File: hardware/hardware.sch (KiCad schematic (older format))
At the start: 5 parts

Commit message: 3.3V Voltage Regulator.
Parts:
- removed U?: L78L05_SOT89, Package_TO_SOT_SMD:SOT-89-3, symbol Regulator_Linear:L78L05_SOT89
- added C2: 0.1μF, symbol Device:C
- added C3: 1μF, symbol Device:C
- added C?: 10μF, symbol Device:CP
- added D?: M7, symbol Device:D
- added R1: 1.5k, symbol Device:R
- added R2: 1k, symbol Device:R
- added U3: LM317A, Package_TO_SOT_SMD:TO-252-2, symbol Regulator_Linear:LM317_3PinPackage
- gave numbers to parts that had none: 4
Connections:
- net labels added: Vdd
- wire segments 20 -> 49
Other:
- note added: "3.3V Voltage Regulator \w Improved Ripple Rejection"
- moved on the sheet: C1, J1, U1, U2

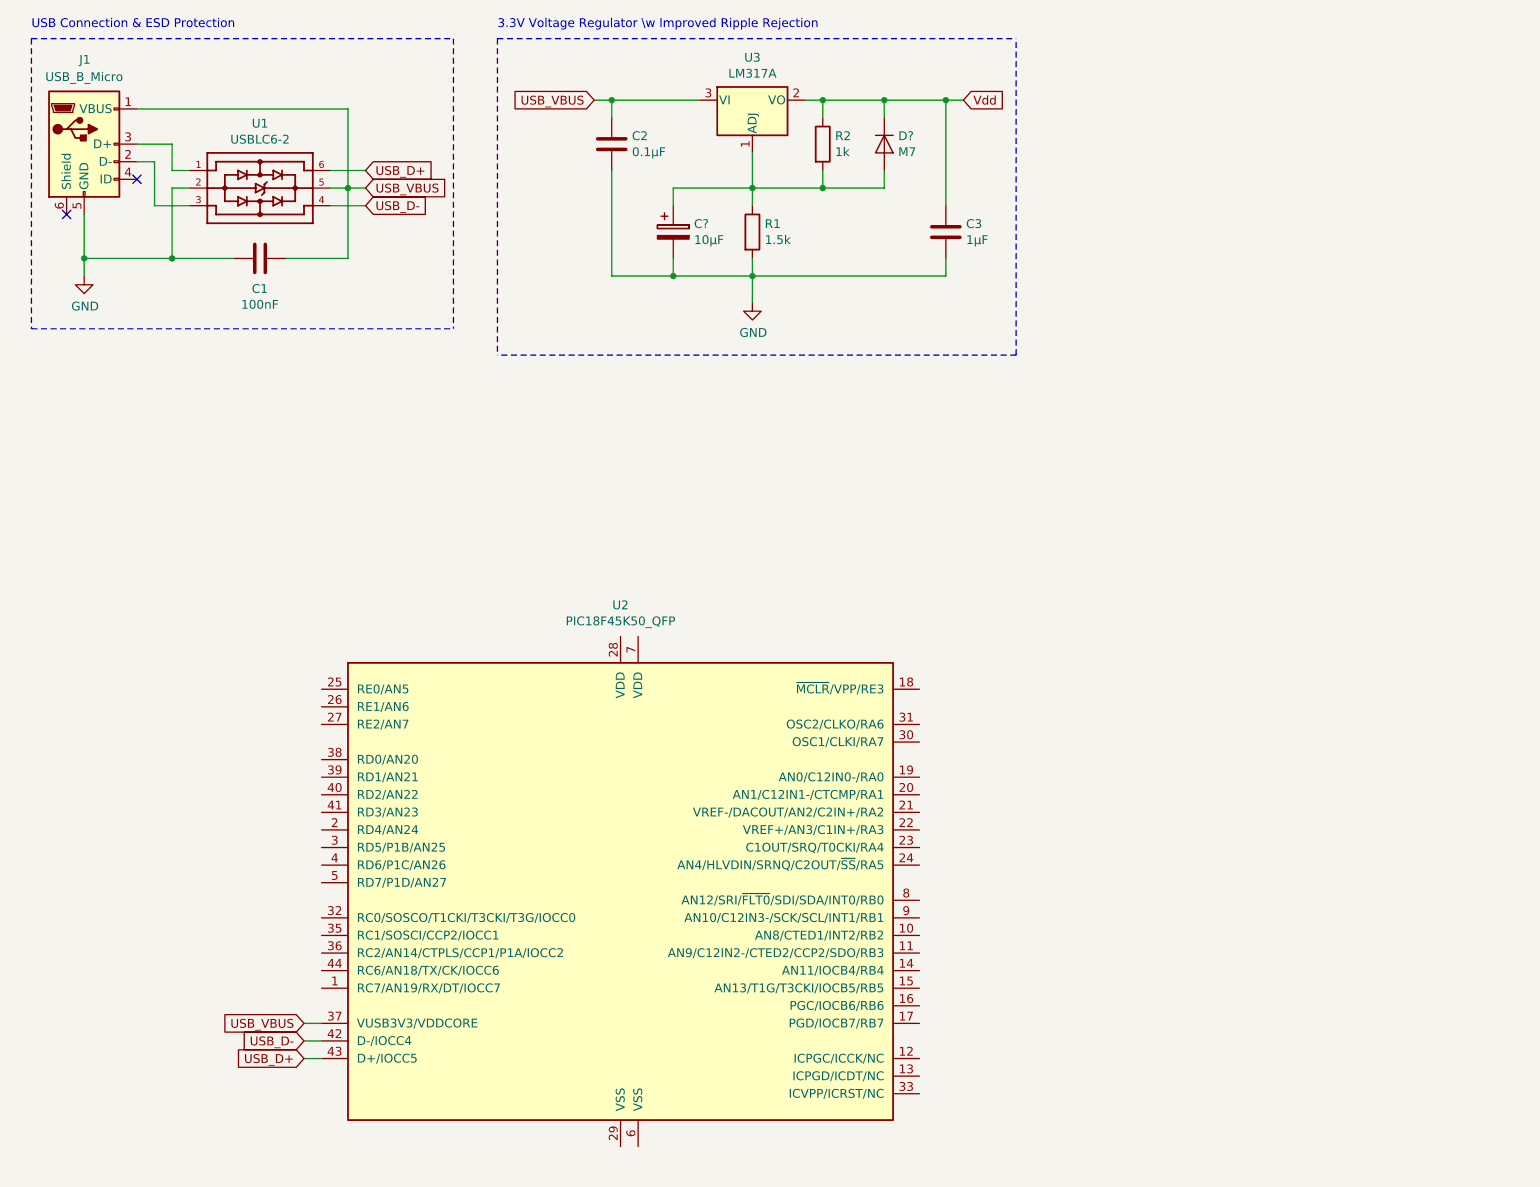
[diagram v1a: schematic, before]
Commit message: Battery protection circuit.
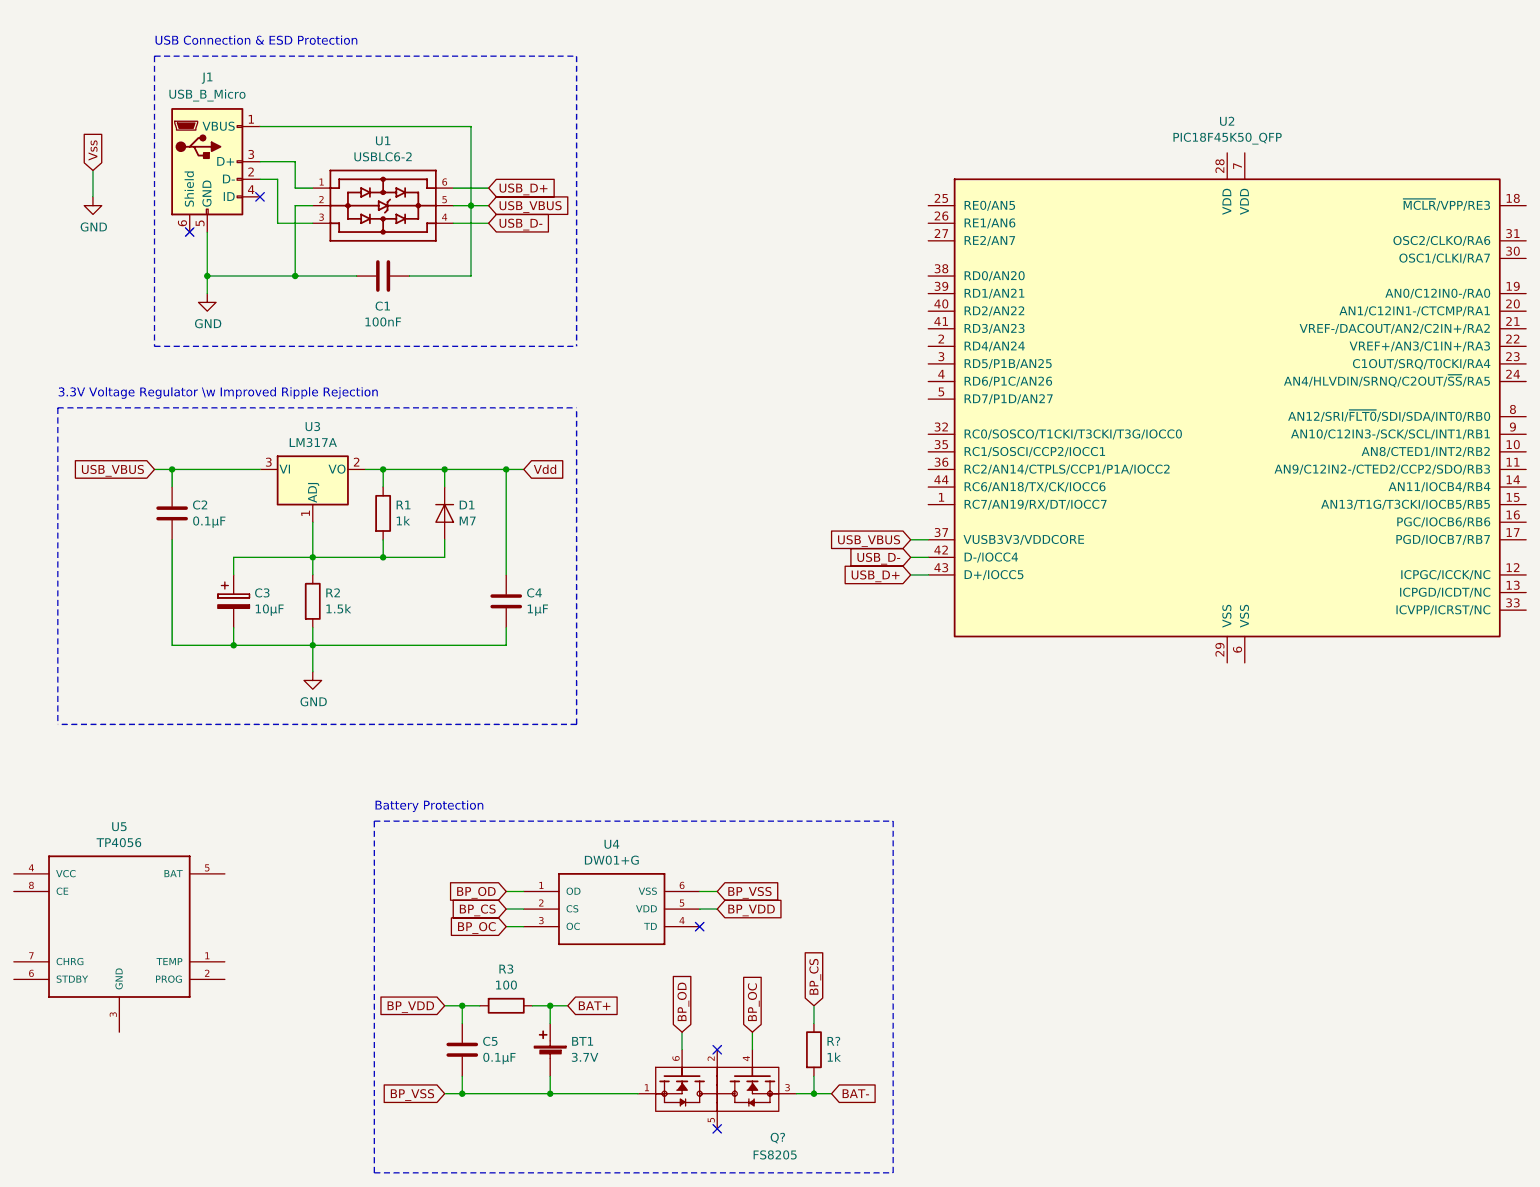
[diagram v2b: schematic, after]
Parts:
- added BT1: 3.7V, symbol Device:Battery_Cell
- added C5: 0.1μF, symbol Device:C
- added Q?: FS8205, Package_TO_SOT_SMD:TSOT-23-6_HandSoldering, symbol Missing:FS8205
- added R3: 100, symbol Device:R
- added R?: 1k, symbol Device:R
- added U4: DW01+G, Package_TO_SOT_SMD:TSOT-23-6_HandSoldering, symbol Missing:DW01
- added U5: TP4056, Package_SO:SSOP-8_2.95x2.8mm_P0.65mm, symbol Missing:TP4056
- gave numbers to parts that had none: 2
- renumbered C3 to C4, R2 to R1, R1 to R2
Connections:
- new net BAT+: BT1.1 (+), R3.1
- new net BAT-: Q?.3, R?.2
- new net BP_CS: R?.1, U4.2 (CS)
- new net BP_OC: Q?.4, U4.3 (OC)
- new net BP_OD: Q?.6, U4.1 (OD)
- new net BP_VDD: C5.1, R3.2, U4.5 (VDD)
- new net BP_VSS: BT1.2 (-), C5.2, Q?.1, U4.6 (VSS)
- no-connect marks 2 -> 5
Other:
- note added: "Battery Protection"
- moved on the sheet: C1, C2, C3, C4, D1, J1, R1, R2, U1, U2, U3

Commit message: Battery management circuit.
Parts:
- added C6, C7: 10μF, symbol Device:C
- added D2: GHC-YR, symbol Device:LED
- added D3: BHC-ZL, symbol Device:LED
- added D4: ZMM5V1, Diode_SMD:D_MiniMELF_Handsoldering, symbol Device:D_Zener
- added R4, R6: 68, symbol Device:R
- added R5: 180, symbol Device:R
- added R7: 2k, symbol Device:R
- gave numbers to parts that had none: 2
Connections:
- net BP_VSS is gone; now on net GND: BT1.2 (-), C5.2, Q1.1, U4.6 (VSS)
- net BAT+: now also R3.2, U5.5 (BAT), C7.1; no longer R3.1
- net BP_VDD: now also C2.1, R3.1, U3.3 (VI); no longer R3.2
- net GND: now also U5.1 (TEMP), U5.3 (GND), C6.2, C7.2, D4.2 (A), R7.2
- net USB_VBUS: now also R5.2; no longer C2.1, U3.3 (VI)
- net at U5.2 (PROG): now also R7.1
- net at U5.4 (VCC): now also U5.8 (CE), C6.1, D2.2 (A), D3.2 (A), D4.1 (K), R5.1
- net at U5.6 (STDBY): now also R4.1
- net at U5.7 (CHRG): now also R6.1
- net BAT-: no longer names the net of Q1.3, R8.2
- new net: D2.1 (K), R4.2
- new net: D3.1 (K), R6.2
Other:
- note added: "580mA Battery Management"
- moved on the sheet: BT1, C1, C2, C3, C4, C5, D1, J1, Q1, R1, R2, R3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

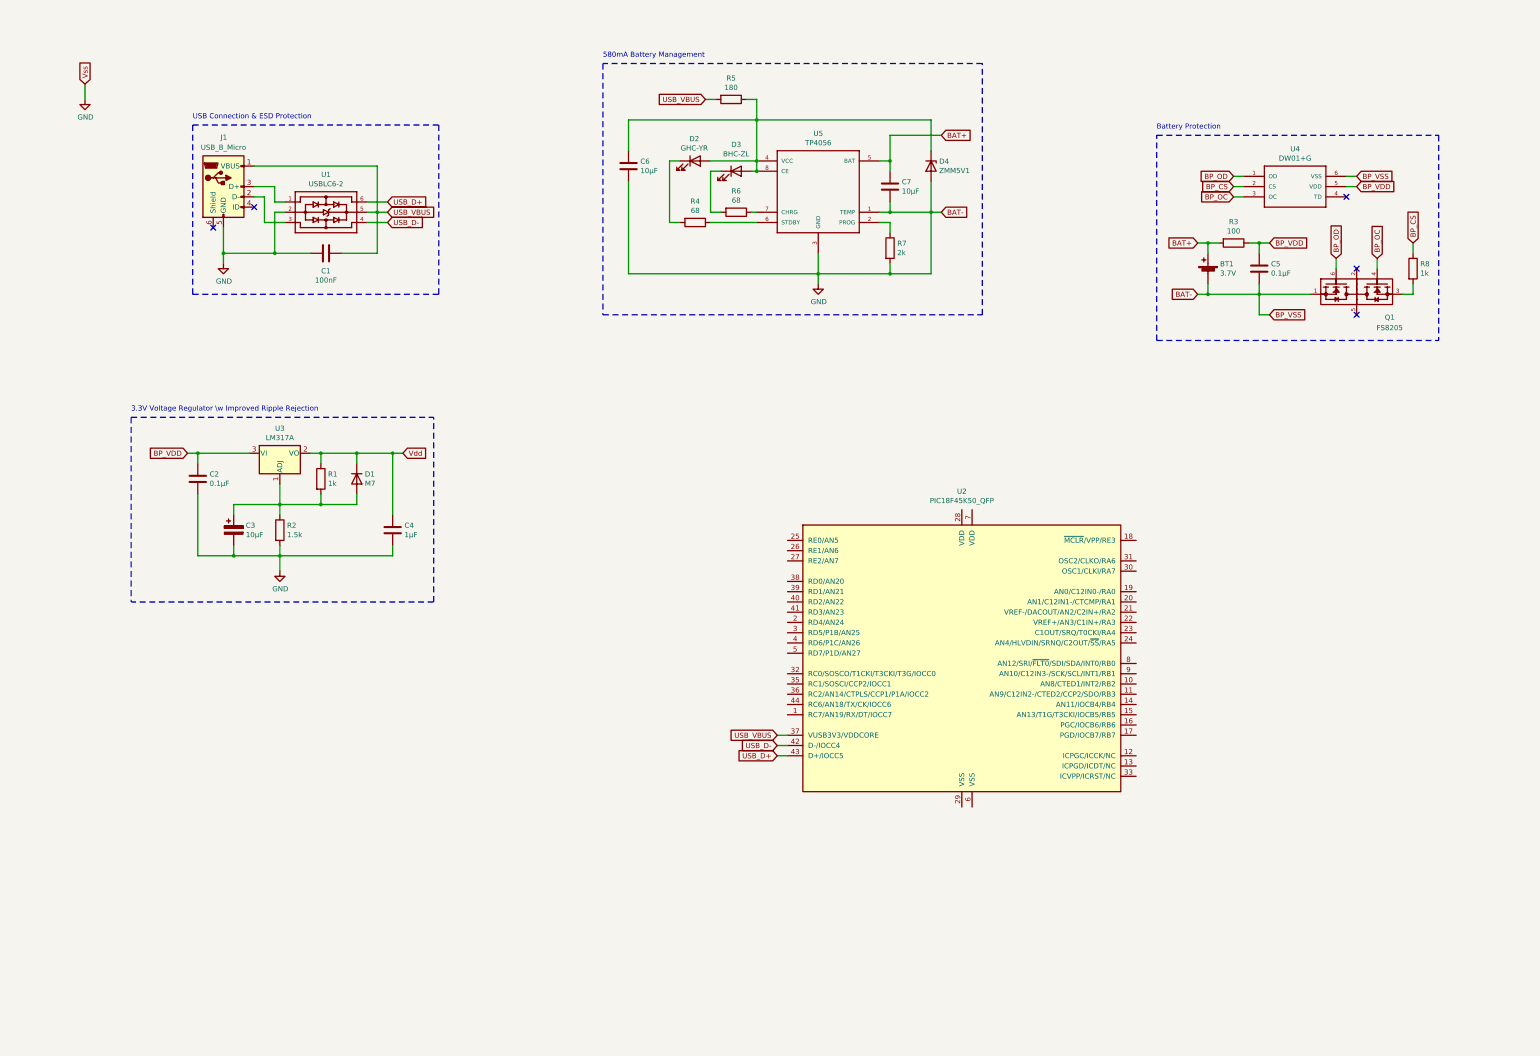
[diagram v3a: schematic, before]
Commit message: Basic MCU wiring for a test batch.
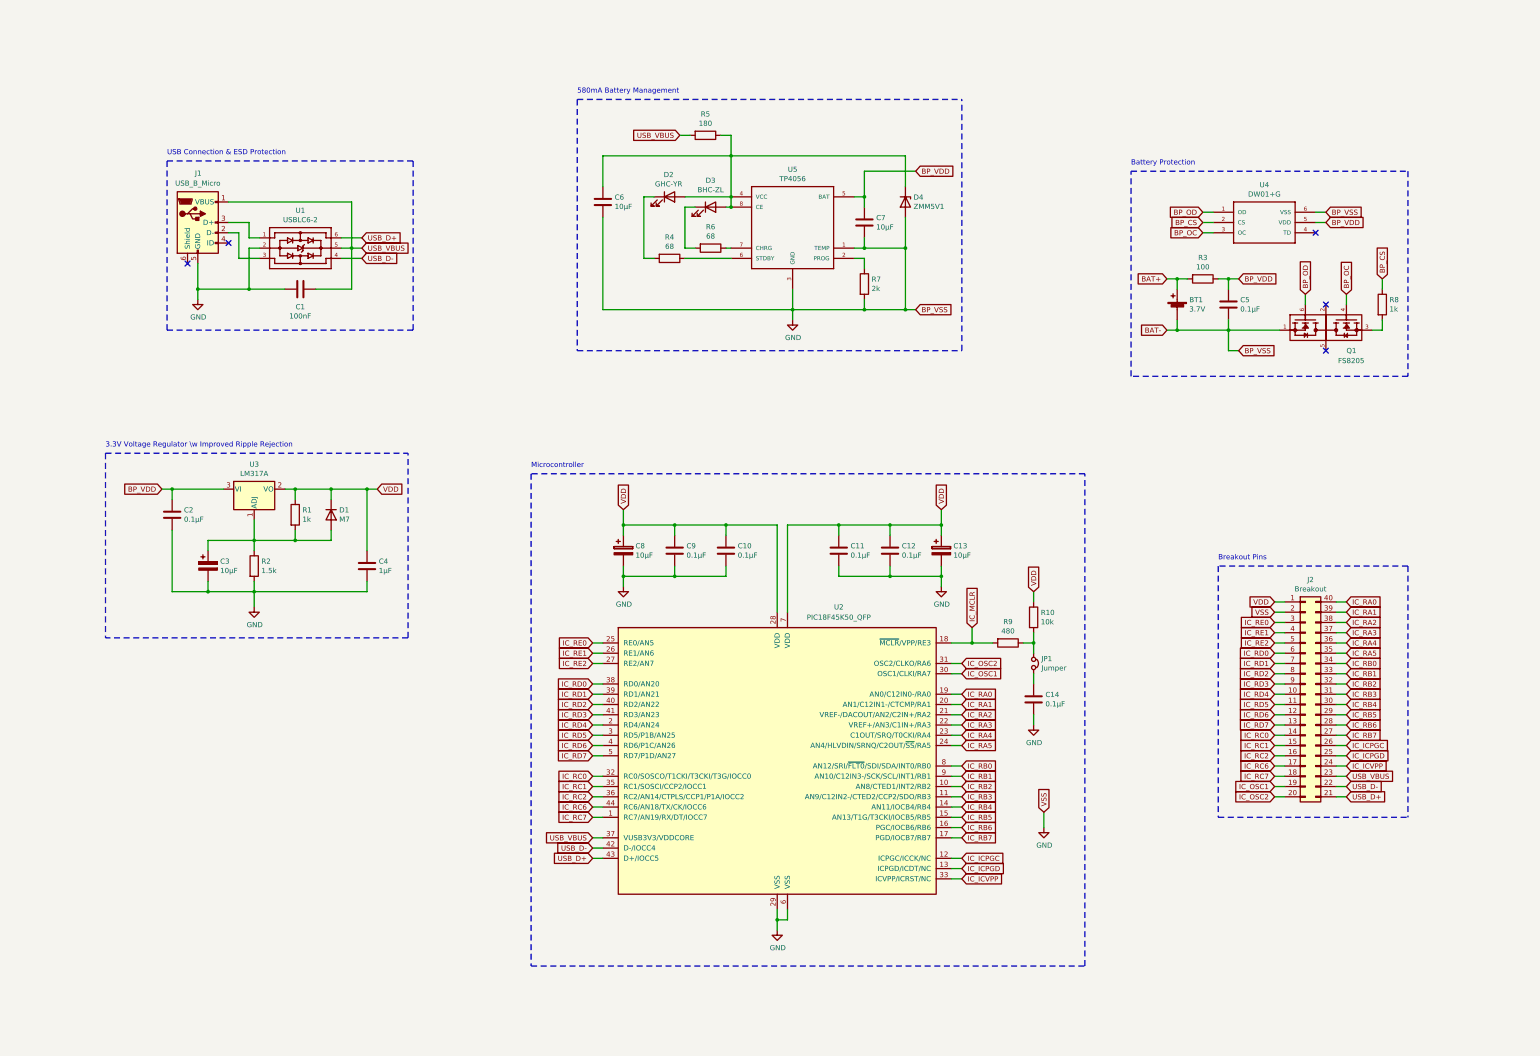
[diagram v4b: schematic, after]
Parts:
- added C10, C11, C12, C14, C9: 0.1μF, symbol Device:C
- added C13, C8: 10μF, symbol Device:CP
- added J2: Breakout, symbol Connector_Generic:Conn_02x20_Counter_Clockwise
- added JP1: Jumper, symbol Device:Jumper_NC_Small
- added R10: 10k, symbol Device:R
- added R9: 480, symbol Device:R
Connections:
- net Vdd is gone; now on net VDD: C4.1, D1.1 (K), R1.1, U3.2 (VO)
- net BAT+: no longer C7.1, U5.5 (BAT)
- net BP_VDD: now also C7.1, U5.5 (BAT)
- net GND: now also U2.29 (VSS), U2.6 (VSS), C10.2, C11.2, C12.2, C13.2, C14.2, C8.2, C9.2, J2.2 (Pin_2)
- net USB_D+: now also J2.21 (Pin_21)
- net USB_D-: now also J2.22 (Pin_22)
- net USB_VBUS: now also J2.23 (Pin_23)
- net IC_RC7: now reaches U2.1 (RC7/AN19/RX/DT/IOCC7)
- net IC_RC7: now also J2.18 (Pin_18)
- net IC_RB2: now reaches U2.10 (AN8/CTED1/INT2/RB2)
- net IC_RB2: now also J2.32 (Pin_32)
- net IC_RB3: now reaches U2.11 (AN9/C12IN2-/CTED2/CCP2/SDO/RB3)
- net IC_RB3: now also J2.31 (Pin_31)
- net IC_ICPGC: now reaches U2.12 (ICPGC/ICCK/NC)
- net IC_ICPGC: now also J2.26 (Pin_26)
- net IC_ICPGD: now reaches U2.13 (ICPGD/ICDT/NC)
- net IC_ICPGD: now also J2.25 (Pin_25)
- net IC_RB4: now reaches U2.14 (AN11/IOCB4/RB4)
- net IC_RB4: now also J2.30 (Pin_30)
- net IC_RB5: now reaches U2.15 (AN13/T1G/T3CKI/IOCB5/RB5)
- net IC_RB5: now also J2.29 (Pin_29)
- net IC_RB6: now reaches U2.16 (PGC/IOCB6/RB6)
- net IC_RB6: now also J2.28 (Pin_28)
- net IC_RB7: now reaches U2.17 (PGD/IOCB7/RB7)
- net IC_RB7: now also J2.27 (Pin_27)
- net IC_MCLR: now reaches U2.18 (~MCLR~/VPP/RE3)
- net IC_MCLR: now also R9.2
- net IC_RA0: now reaches U2.19 (AN0/C12IN0-/RA0)
- net IC_RA0: now also J2.40 (Pin_40)
- net IC_RD4: now reaches U2.2 (RD4/AN24)
- net IC_RD4: now also J2.10 (Pin_10)
- net IC_RA1: now reaches U2.20 (AN1/C12IN1-/CTCMP/RA1)
- net IC_RA1: now also J2.39 (Pin_39)
- net IC_RA2: now reaches U2.21 (VREF-/DACOUT/AN2/C2IN+/RA2)
- net IC_RA2: now also J2.38 (Pin_38)
- net IC_RA3: now reaches U2.22 (VREF+/AN3/C1IN+/RA3)
- net IC_RA3: now also J2.37 (Pin_37)
- net IC_RA4: now reaches U2.23 (C1OUT/SRQ/T0CKI/RA4)
- net IC_RA4: now also J2.36 (Pin_36)
- net IC_RA5: now reaches U2.24 (AN4/HLVDIN/SRNQ/C2OUT/~SS~/RA5)
- net IC_RA5: now also J2.35 (Pin_35)
- net IC_RE0: now reaches U2.25 (RE0/AN5)
- net IC_RE0: now also J2.3 (Pin_3)
- net IC_RE1: now reaches U2.26 (RE1/AN6)
- net IC_RE1: now also J2.4 (Pin_4)
- net IC_RE2: now reaches U2.27 (RE2/AN7)
- net IC_RE2: now also J2.5 (Pin_5)
- net VDD: now reaches U2.28 (VDD)
- net VDD: now also U2.7 (VDD), C10.1, C11.1, C12.1, C13.1, C8.1, C9.1, J2.1 (Pin_1), R10.1
- net IC_RD5: now reaches U2.3 (RD5/P1B/AN25)
- net IC_RD5: now also J2.11 (Pin_11)
- net IC_OSC1: now reaches U2.30 (OSC1/CLKI/RA7)
- net IC_OSC1: now also J2.19 (Pin_19)
- net IC_OSC2: now reaches U2.31 (OSC2/CLKO/RA6)
- net IC_OSC2: now also J2.20 (Pin_20)
- net IC_RC0: now reaches U2.32 (RC0/SOSCO/T1CKI/T3CKI/T3G/IOCC0)
- net IC_RC0: now also J2.14 (Pin_14)
- net IC_ICVPP: now reaches U2.33 (ICVPP/ICRST/NC)
- net IC_ICVPP: now also J2.24 (Pin_24)
- net IC_RC1: now reaches U2.35 (RC1/SOSCI/CCP2/IOCC1)
- net IC_RC1: now also J2.15 (Pin_15)
- net IC_RC2: now reaches U2.36 (RC2/AN14/CTPLS/CCP1/P1A/IOCC2)
- net IC_RC2: now also J2.16 (Pin_16)
- net IC_RD0: now reaches U2.38 (RD0/AN20)
- net IC_RD0: now also J2.6 (Pin_6)
- net IC_RD1: now reaches U2.39 (RD1/AN21)
- net IC_RD1: now also J2.7 (Pin_7)
- net IC_RD6: now reaches U2.4 (RD6/P1C/AN26)
- net IC_RD6: now also J2.12 (Pin_12)
- net IC_RD2: now reaches U2.40 (RD2/AN22)
- net IC_RD2: now also J2.8 (Pin_8)
- net IC_RD3: now reaches U2.41 (RD3/AN23)
- net IC_RD3: now also J2.9 (Pin_9)
- net IC_RC6: now reaches U2.44 (RC6/AN18/TX/CK/IOCC6)
- net IC_RC6: now also J2.17 (Pin_17)
- net IC_RD7: now reaches U2.5 (RD7/P1D/AN27)
- net IC_RD7: now also J2.13 (Pin_13)
- net IC_RB0: now reaches U2.8 (AN12/SRI/~FLT0~/SDI/SDA/INT0/RB0)
- net IC_RB0: now also J2.34 (Pin_34)
- net IC_RB1: now reaches U2.9 (AN10/C12IN3-/SCK/SCL/INT1/RB1)
- net IC_RB1: now also J2.33 (Pin_33)
- new net: JP1.1, R10.2, R9.1
- new net: C14.1, JP1.2
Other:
- note added: "Breakout Pins"
- note added: "Microcontroller"
- moved on the sheet: BT1, C1, C2, C3, C4, C5, C6, C7, D1, D2, D3, D4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
